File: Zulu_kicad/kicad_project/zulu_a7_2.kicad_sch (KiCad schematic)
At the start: 36 parts, among them J1 Pmod 2x6, X2 ZULU-CONN

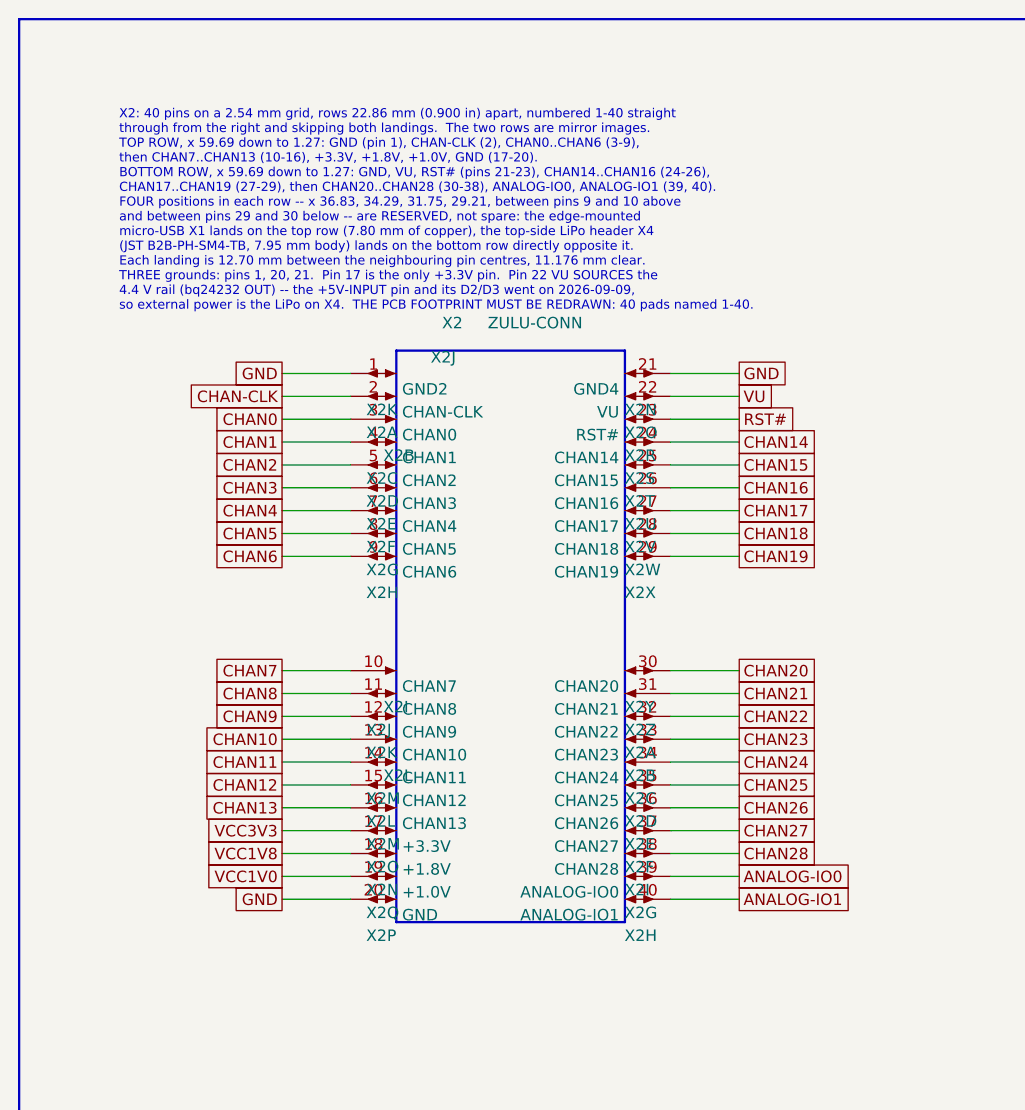
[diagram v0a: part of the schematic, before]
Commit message: X2 power pins re-ordered on all copies; HDI copy gets the X1 land fix
X2 top row, at the user's request: 17 GND, 18 VCC3V3, 19 VCC1V8, 20 VCC1V0
(was 17 VCC3V3, 18 VCC1V8, 19 VCC1V0, 20 GND); pin 16 CHAN13 unchanged.

Altium (production and HDI_Optimized):
- zulu_a7_2.SchDoc via tools/x2_power_pins.py: four gate copies moved with
  their wires and labels, pins renumbered in all 41 copies, NOTE and frame
  reworded.
- PcbDoc via tools/X2PowerPins.pas: pads re-netted, VCC1V8 L3 stub moved to
  pin 19, VCC1V0 Bottom run extended to pin 20, planes repoured. ECO preview
  shows no net changes; only the X2 NOTE was imported.
- Post-save DRC 0/0 (production 14:28, HDI 14:34). Drill files
  byte-identical; copper differs only at X2's corner.
- Gerbers, drills, fab notes, zips and assembly notes/drawings regenerated;
  BOM and CPL unchanged.
- Production PcbDoc 517b553e, PCBWay zip FD44329E.
- HDI PcbDoc 71e75c10, zips 9C3E89E2 (JLC) / B679B6A3 (PCBWay).

KiCad: tools/apply_x2_pins_sch.py and apply_x2_pins_pcb.py. Netlist differs
in exactly the four pins, geometry identical to the Altium import, parity 0,
unconnected 0; reports regenerated.

HDI_Optimized also gets the X1 MS1/MS2 land and clearance fix (HdiX1Pads,
HdiX1Rules, HdiX1Lib): oblong 1.11x1.81 / 0.90x1.60 lands, CHAN12 re-routed
over the slots, PcbLib footprint updated. Fab notes now give the buried-via
land as 0.27 mm.

Master BOM regenerated: X2 note, and the 0.1 uF line gains C155-C159.

Co-Authored-By: Claude Opus 5.5 <noreply@anthropic.com>
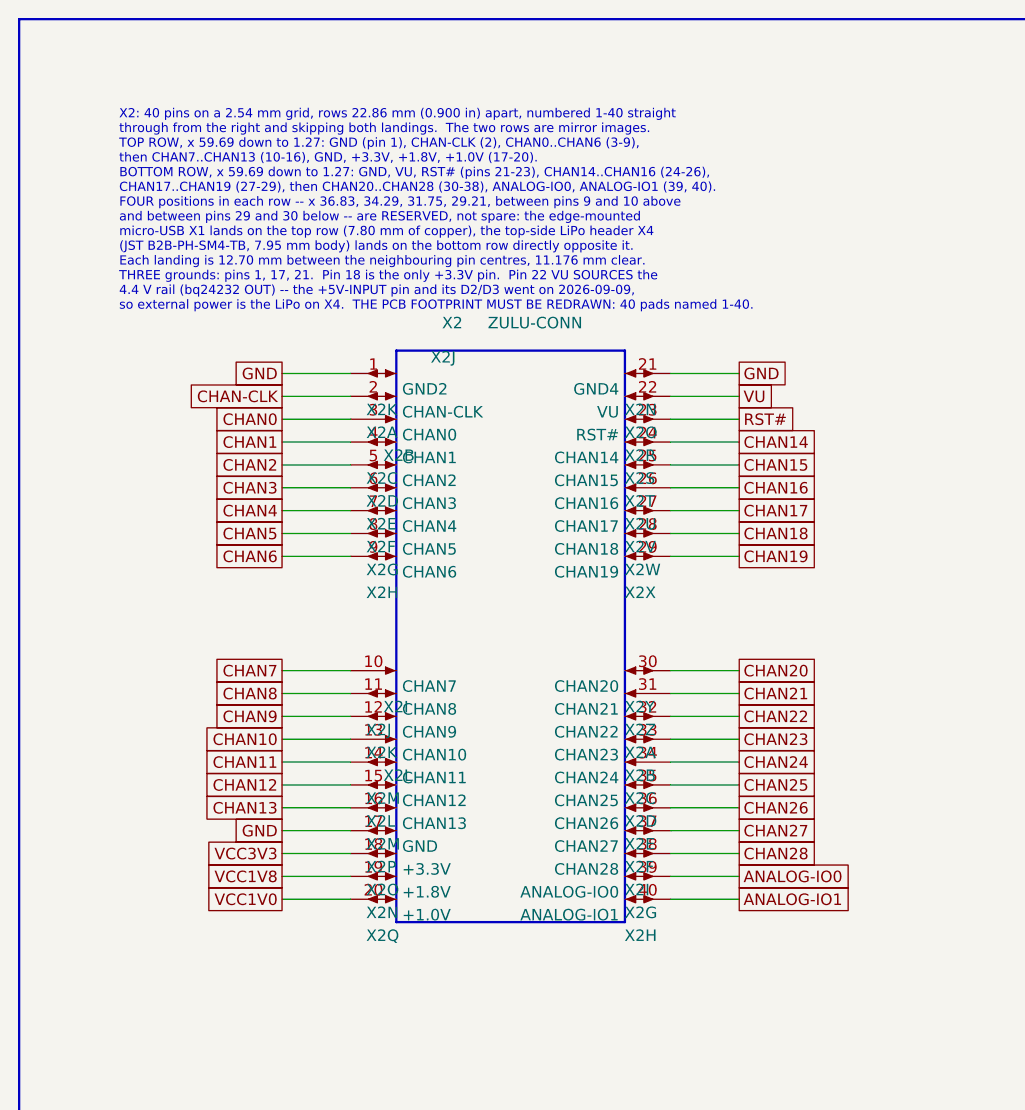
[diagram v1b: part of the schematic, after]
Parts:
- X2: NOTE Pin field ZULU-DIP37: 40 pins of 1.016 mm on 2.54 mm pitch, two rows 22.86 mm (0.900 in) apart, numbered 1-40 straight through and skipping both landings. The rows are mirror images: top row pins 1-9 (x 59.69..39.37) = GND, CHAN-CLK, CHAN0..CHAN6, FOUR positions for the micro-USB X1 (36.83..29.21), pins 10-20 (26.67..1.27) = CHAN7..CHAN13, +3.3V, +1.8V, +1.0V, GND, in channel order since 2026-09-09; bottom row pins 21-29 (59.69..39.37), FOUR positions for the LiPo header X4 at the SAME four x values (36.83..29.21), pins 30-40 (26.67..1.27), so X4 sits on the top side directly opposite the edge-mounted USB receptacle. Each landing is 12.70 mm between the neighbouring pin centres, 11.176 mm clear: the JST B2B-PH-SM4-TB body is 7.95 mm, so 1.61 mm each side. Reworked 2026-09-09 from the old 44-position pattern: +5V-INPUT with D2/D3, GND5, GND3 and +3.3V2 removed, CHAN12/CHAN13 moved to pins 2/3, the bottom row closed up, the field renumbered and the landing moved. Three grounds (1, 20, 2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 -> Pin field ZULU-DIP37: 40 pins of 1.016 mm on 2.54 mm pitch, two rows 22.86 mm (0.900 in) apart, numbered 1-40 straight through and skipping both landings. The rows are mirror images: top row pins 1-9 (x 59.69..39.37) = GND, CHAN-CLK, CHAN0..CHAN6, FOUR positions for the micro-USB X1 (36.83..29.21), pins 10-20 (26.67..1.27) = CHAN7..CHAN13, GND, +3.3V, +1.8V, +1.0V (channel order since 2026-09-09, power pins re-ordered 2026-10-07); bottom row pins 21-29 (59.69..39.37), FOUR positions for the LiPo header X4 at the SAME four x values (36.83..29.21), pins 30-40 (26.67..1.27), so X4 sits on the top side directly opposite the edge-mounted USB receptacle. Each landing is 12.70 mm between the neighbouring pin centres, 11.176 mm clear: the JST B2B-PH-SM4-TB body is 7.95 mm, so 1.61 mm each side. Reworked 2026-09-09 from the old 44-position pattern: +5V-INPUT with D2/D3, GND5, GND3 and +3.3V2 removed, CHAN12/CHAN13 moved to pins 2/3, the bottom row closed up, the field renumbered and the landin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
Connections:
- net GND: now also X2.17 (1); no longer X2.20 (1)
- net VCC1V0: now also X2.20 (1); no longer X2.19 (1)
- net VCC1V8: now also X2.19 (1); no longer X2.18 (1)
- net VCC3V3: now also X2.18 (1); no longer X2.17 (1)
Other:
- moved on the sheet: X2N, X2O, X2P, X2Q

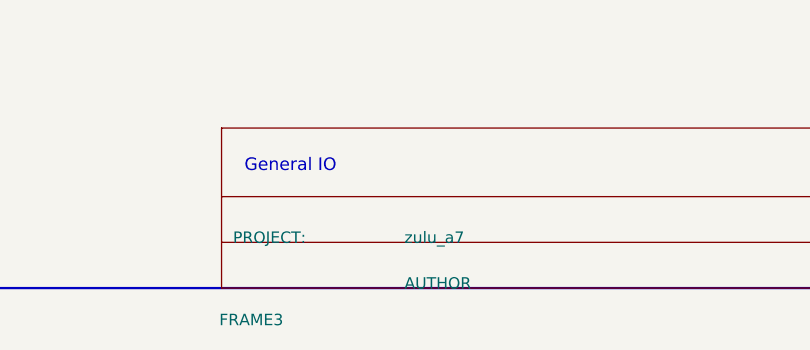
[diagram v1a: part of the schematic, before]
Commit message: Show "AUTHOR: Christian Tambe" in every schematic title block
The EAGLE title block reads "AUTHOR: >AUTHOR" (>AUTHOR = Christian Tambe).
The Altium EAGLE importer left the DOCFIELD AUTHOR parameter as the
literal word "AUTHOR" and dropped the "AUTHOR:" label, and the KiCad
conversion inherited the placeholder.

- Altium (production and HDI_Optimized, 7 SchDocs each):
  tools/schematic_author.py sets the AUTHOR parameter to "Christian Tambe"
  and appends an "AUTHOR:" label at the PROJECT: column in its font, then
  updates the header Weight; every other record stays byte-identical.
  Checked in Altium (sheets 1 and 3) and with the ECO preview, which shows
  only the usual never-executed baseline.
- KiCad: tools/apply_schematic_author.py sets the AUTHOR property and adds
  an AUTHOR_LABEL property. PDF plot shows the row on all 7 pages; netlist
  identical, ERC 1,648 unchanged.
- Docs: docs/schematic_author.md, HDI notes, CONVERSION.md, README notices.
  Zulu_Altrium/ and Altium_backup/ are left as historical snapshots.

Co-Authored-By: Claude Opus 5.5 <noreply@anthropic.com>
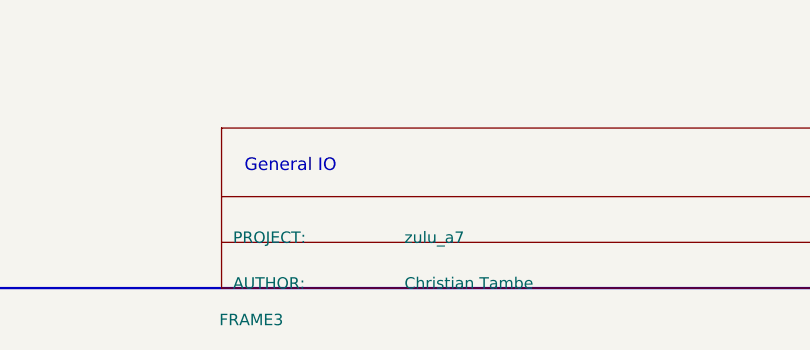
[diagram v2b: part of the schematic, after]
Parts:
- FRAME3: AUTHOR AUTHOR -> Christian Tambe; AUTHOR_LABEL (none) -> AUTHOR:
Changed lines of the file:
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@@
 			)
 		)
-		(property "AUTHOR" "AUTHOR"
+		(property "AUTHOR" "Christian Tambe"
 			(at 116.84 315.976 90)
 			(show_name no)
 			(do_not_autoplace no)
+			(effects
+				(font
+					(size 1.27 1.27)
+				)
+				(justify right bottom)
+			)
+		)
+		(property "AUTHOR_LABEL" "AUTHOR:"
+			(at 97.79 315.976 90)
+			(show_name no)
+			(do_not_autoplace no)
